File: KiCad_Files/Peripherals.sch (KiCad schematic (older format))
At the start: 20 parts, among them J3 MEM2075-00-140-01-A, U2 TCAN330G, U3 W25Q32JVSSIQ_TR

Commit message: Revert "Add shapes3D folder again"
This reverts commit 7987a310af828f940c17547aa6162ac2ebe2b018.
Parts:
- C11, C12, C13, C14, C15, C16, C17, C18, C19: symbol archive:Device_C_Small -> Device:C_Small
- D2: symbol archive:dk_TVS-Diodes_PESD2CAN_215 -> dk_TVS-Diodes:PESD2CAN_215
- J3: symbol archive:SamacSys_Parts_MEM2075-00-140-01-A -> SamacSys_Parts:MEM2075-00-140-01-A
- R5, R6, R7, R8, R9: symbol archive:Device_R_Small -> Device:R_Small
- RN1, RN2: symbol archive:Device_R_Pack04 -> Device:R_Pack04
- U2: symbol archive:Interface_CAN_LIN_TCAN330G -> Interface_CAN_LIN:TCAN330G
- U3: symbol archive:dk_Memory_W25Q32JVSSIQ_TR -> dk_Memory:W25Q32JVSSIQ_TR
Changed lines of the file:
@@
 $EndDescr
 $Comp
-L archive:power_+3.3V #PWR0115
+L power:+3.3V #PWR0115
 U 1 1 616DD3D7
 P 4400 5025
@@
 	4400 5025 4400 5100
 $Comp
-L archive:power_GND #PWR0119
+L power:GND #PWR0119
 U 1 1 616E5BF7
 P 4400 6750
@@
 	4400 6750 4400 6700
 $Comp
-L archive:Device_R_Pack04 RN2
+L Device:R_Pack04 RN2
 U 1 1 616ED35C
 P 3350 5425
@@
 	3550 5225 3550 5175
 $Comp
-L archive:power_+3.3V #PWR0120
+L power:+3.3V #PWR0120
 U 1 1 616ED34A
 P 3400 5100
@@
 $EndComp
 $Comp
-L archive:Device_R_Pack04 RN1
+L Device:R_Pack04 RN1
 U 1 1 616D8B8F
 P 2875 5425
@@
 	3075 5225 3075 5175
 $Comp
-L archive:power_+3.3V #PWR0121
+L power:+3.3V #PWR0121
 U 1 1 616DBD2E
 P 2925 5100
@@
 $EndComp
 $Comp
-L archive:Device_C_Small C17
+L Device:C_Small C17
 U 1 1 616FE025
 P 4600 5250
@@
 Connection ~ 4400 5100
 $Comp
-L archive:power_GND #PWR0122
+L power:GND #PWR0122
 U 1 1 616FF326
 P 4600 5450
@@
 SD_CARD_CD
 $Comp
-L archive:dk_Memory_W25Q32JVSSIQ_TR U3
+L dk_Memory:W25Q32JVSSIQ_TR U3
 U 1 1 614419FF
 P 9375 3825
@@
 $EndComp
 $Comp
-L archive:power_+3.3V #PWR0123
+L power:+3.3V #PWR0123
 U 1 1 6144F897
 P 9325 2925
@@
 $EndComp
 $Comp
-L archive:Device_C_Small C19
+L Device:C_Small C19
 U 1 1 6144FF8B
 P 9475 3125
@@
 $EndComp
 $Comp
-L archive:power_GND #PWR0124
+L power:GND #PWR0124
 U 1 1 61450343
 P 9475 3275
@@
 Connection ~ 9325 2975
 $Comp
-L archive:power_GND #PWR0125
+L power:GND #PWR0125
 U 1 1 6145B8A8
 P 9325 4325
@@
 	9325 4325 9325 4225
 $Comp
-L archive:Device_R_Small R9
+L Device:R_Small R9
 U 1 1 6145D636
 P 8825 3300
@@
 	9675 3875 9750 3875
 $Comp
-L archive:Device_C_Small C18
+L Device:C_Small C18
 U 1 1 61EAA5F8
 P 4975 5250
@@
 	4400 5100 4400 5500
 $Comp
-L archive:SamacSys_Parts_MEM2075-00-140-01-A J3
+L SamacSys_Parts:MEM2075-00-140-01-A J3
 U 1 1 616CDB72
 P 3750 5800
@@
 	3350 5175 3250 5175
 $Comp
-L archive:power_+3.3V #PWR0126
+L power:+3.3V #PWR0126
 U 1 1 61595989
 P 9750 3650
@@
 	9750 3650 9750 3775
 $Comp
-L archive:Interface_CAN_LIN_TCAN330G U2
+L Interface_CAN_LIN:TCAN330G U2
 U 1 1 61FFDC40
 P 3075 2425
@@
 $EndComp
 $Comp
-L archive:power_+3.3V #PWR0127
+L power:+3.3V #PWR0127
 U 1 1 620360A4
 P 3075 1425
@@
 $EndComp
 $Comp
-L archive:Device_C_Small C12
+L Device:C_Small C12
 U 1 1 620360AA
 P 3275 1625
@@
 	3275 1475 3275 1525
 $Comp
-L archive:power_GND #PWR0128
+L power:GND #PWR0128
 U 1 1 620360B2
 P 3275 1825
@@
 $EndComp
 $Comp
-L archive:Device_C_Small C13
+L Device:C_Small C13
 U 1 1 620360B8
 P 3650 1625
@@
 	3075 2900 3075 2825
 $Comp
-L archive:power_GND #PWR0129
+L power:GND #PWR0129
 U 1 1 6203C3B0
 P 3075 2900
@@
 $EndComp
 $Comp
-L archive:Device_R_Small R5
+L Device:R_Small R5
 U 1 1 620499E0
 P 2275 1875
@@
 $EndComp
 $Comp
-L archive:Device_R_Small R6
+L Device:R_Small R6
 U 1 1 620499E6
 P 2275 1975
@@
 CAN_RXD
 $Comp
-L archive:Device_C_Small C11
+L Device:C_Small C11
 U 1 1 620499EE
 P 2050 2150
@@
 $EndComp
 $Comp
-L archive:power_GND #PWR0130
+L power:GND #PWR0130
 U 1 1 620499F4
 P 2050 2275
@@
 CAN_H
 $Comp
-L archive:Device_R_Small R7
+L Device:R_Small R7
 U 1 1 62072AC4
 P 3800 2250
@@
 $EndComp
 $Comp
-L archive:Device_R_Small R8
+L Device:R_Small R8
 U 1 1 62072ACA
 P 3800 2650
@@
 	3800 2450 3800 2550
 $Comp
-L archive:Device_C_Small C16
+L Device:C_Small C16
 U 1 1 62072AD8
 P 4425 3000
@@
 $EndComp
 $Comp
-L archive:power_GND #PWR0131
+L power:GND #PWR0131
 U 1 1 62072ADE
 P 4425 3125
@@
 	4075 2450 3800 2450
 $Comp
-L archive:power_GND #PWR0132
+L power:GND #PWR0132
 U 1 1 62072AE8
 P 4075 2675
@@
 $EndComp
 $Comp
-L archive:Device_C_Small C14
+L Device:C_Small C14
 U 1 1 62072AEE
 P 4075 2575
@@
 CAN_L
 $Comp
-L archive:power_GND #PWR0133
+L power:GND #PWR0133
 U 1 1 62072B00
 P 4425 2325
@@
 	4425 2325 4425 2300
 $Comp
-L archive:Device_C_Small C15
+L Device:C_Small C15
 U 1 1 62072B07
 P 4425 2200
@@
 	3800 2050 4425 2050
 $Comp
-L archive:dk_TVS-Diodes_PESD2CAN_215 D2
+L dk_TVS-Diodes:PESD2CAN_215 D2
 U 1 1 62072B1A
 P 5075 2450
@@
 	4725 2850 5350 2850
 $Comp
-L archive:power_GND #PWR0134
+L power:GND #PWR0134
 U 1 1 62072B28
 P 5450 2500

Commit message: Archive Schematic
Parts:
- C11, C12, C13, C14, C15, C16, C17, C18, C19: symbol Device:C_Small -> archive:Device_C_Small
- D2: symbol dk_TVS-Diodes:PESD2CAN_215 -> archive:dk_TVS-Diodes_PESD2CAN_215
- J3: symbol SamacSys_Parts:MEM2075-00-140-01-A -> archive:SamacSys_Parts_MEM2075-00-140-01-A
- R5, R6, R7, R8, R9: symbol Device:R_Small -> archive:Device_R_Small
- RN1, RN2: symbol Device:R_Pack04 -> archive:Device_R_Pack04
- U2: symbol Interface_CAN_LIN:TCAN330G -> archive:Interface_CAN_LIN_TCAN330G
- U3: symbol dk_Memory:W25Q32JVSSIQ_TR -> archive:dk_Memory_W25Q32JVSSIQ_TR
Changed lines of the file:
@@
 $EndDescr
 $Comp
-L power:+3.3V #PWR0115
+L archive:power_+3.3V #PWR0115
 U 1 1 616DD3D7
 P 4400 5025
@@
 	4400 5025 4400 5100
 $Comp
-L power:GND #PWR0119
+L archive:power_GND #PWR0119
 U 1 1 616E5BF7
 P 4400 6750
@@
 	4400 6750 4400 6700
 $Comp
-L Device:R_Pack04 RN2
+L archive:Device_R_Pack04 RN2
 U 1 1 616ED35C
 P 3350 5425
@@
 	3550 5225 3550 5175
 $Comp
-L power:+3.3V #PWR0120
+L archive:power_+3.3V #PWR0120
 U 1 1 616ED34A
 P 3400 5100
@@
 $EndComp
 $Comp
-L Device:R_Pack04 RN1
+L archive:Device_R_Pack04 RN1
 U 1 1 616D8B8F
 P 2875 5425
@@
 	3075 5225 3075 5175
 $Comp
-L power:+3.3V #PWR0121
+L archive:power_+3.3V #PWR0121
 U 1 1 616DBD2E
 P 2925 5100
@@
 $EndComp
 $Comp
-L Device:C_Small C17
+L archive:Device_C_Small C17
 U 1 1 616FE025
 P 4600 5250
@@
 Connection ~ 4400 5100
 $Comp
-L power:GND #PWR0122
+L archive:power_GND #PWR0122
 U 1 1 616FF326
 P 4600 5450
@@
 SD_CARD_CD
 $Comp
-L dk_Memory:W25Q32JVSSIQ_TR U3
+L archive:dk_Memory_W25Q32JVSSIQ_TR U3
 U 1 1 614419FF
 P 9375 3825
@@
 $EndComp
 $Comp
-L power:+3.3V #PWR0123
+L archive:power_+3.3V #PWR0123
 U 1 1 6144F897
 P 9325 2925
@@
 $EndComp
 $Comp
-L Device:C_Small C19
+L archive:Device_C_Small C19
 U 1 1 6144FF8B
 P 9475 3125
@@
 $EndComp
 $Comp
-L power:GND #PWR0124
+L archive:power_GND #PWR0124
 U 1 1 61450343
 P 9475 3275
@@
 Connection ~ 9325 2975
 $Comp
-L power:GND #PWR0125
+L archive:power_GND #PWR0125
 U 1 1 6145B8A8
 P 9325 4325
@@
 	9325 4325 9325 4225
 $Comp
-L Device:R_Small R9
+L archive:Device_R_Small R9
 U 1 1 6145D636
 P 8825 3300
@@
 	9675 3875 9750 3875
 $Comp
-L Device:C_Small C18
+L archive:Device_C_Small C18
 U 1 1 61EAA5F8
 P 4975 5250
@@
 	4400 5100 4400 5500
 $Comp
-L SamacSys_Parts:MEM2075-00-140-01-A J3
+L archive:SamacSys_Parts_MEM2075-00-140-01-A J3
 U 1 1 616CDB72
 P 3750 5800
@@
 	3350 5175 3250 5175
 $Comp
-L power:+3.3V #PWR0126
+L archive:power_+3.3V #PWR0126
 U 1 1 61595989
 P 9750 3650
@@
 	9750 3650 9750 3775
 $Comp
-L Interface_CAN_LIN:TCAN330G U2
+L archive:Interface_CAN_LIN_TCAN330G U2
 U 1 1 61FFDC40
 P 3075 2425
@@
 $EndComp
 $Comp
-L power:+3.3V #PWR0127
+L archive:power_+3.3V #PWR0127
 U 1 1 620360A4
 P 3075 1425
@@
 $EndComp
 $Comp
-L Device:C_Small C12
+L archive:Device_C_Small C12
 U 1 1 620360AA
 P 3275 1625
@@
 	3275 1475 3275 1525
 $Comp
-L power:GND #PWR0128
+L archive:power_GND #PWR0128
 U 1 1 620360B2
 P 3275 1825
@@
 $EndComp
 $Comp
-L Device:C_Small C13
+L archive:Device_C_Small C13
 U 1 1 620360B8
 P 3650 1625
@@
 	3075 2900 3075 2825
 $Comp
-L power:GND #PWR0129
+L archive:power_GND #PWR0129
 U 1 1 6203C3B0
 P 3075 2900
@@
 $EndComp
 $Comp
-L Device:R_Small R5
+L archive:Device_R_Small R5
 U 1 1 620499E0
 P 2275 1875
@@
 $EndComp
 $Comp
-L Device:R_Small R6
+L archive:Device_R_Small R6
 U 1 1 620499E6
 P 2275 1975
@@
 CAN_RXD
 $Comp
-L Device:C_Small C11
+L archive:Device_C_Small C11
 U 1 1 620499EE
 P 2050 2150
@@
 $EndComp
 $Comp
-L power:GND #PWR0130
+L archive:power_GND #PWR0130
 U 1 1 620499F4
 P 2050 2275
@@
 CAN_H
 $Comp
-L Device:R_Small R7
+L archive:Device_R_Small R7
 U 1 1 62072AC4
 P 3800 2250
@@
 $EndComp
 $Comp
-L Device:R_Small R8
+L archive:Device_R_Small R8
 U 1 1 62072ACA
 P 3800 2650
@@
 	3800 2450 3800 2550
 $Comp
-L Device:C_Small C16
+L archive:Device_C_Small C16
 U 1 1 62072AD8
 P 4425 3000
@@
 $EndComp
 $Comp
-L power:GND #PWR0131
+L archive:power_GND #PWR0131
 U 1 1 62072ADE
 P 4425 3125
@@
 	4075 2450 3800 2450
 $Comp
-L power:GND #PWR0132
+L archive:power_GND #PWR0132
 U 1 1 62072AE8
 P 4075 2675
@@
 $EndComp
 $Comp
-L Device:C_Small C14
+L archive:Device_C_Small C14
 U 1 1 62072AEE
 P 4075 2575
@@
 CAN_L
 $Comp
-L power:GND #PWR0133
+L archive:power_GND #PWR0133
 U 1 1 62072B00
 P 4425 2325
@@
 	4425 2325 4425 2300
 $Comp
-L Device:C_Small C15
+L archive:Device_C_Small C15
 U 1 1 62072B07
 P 4425 2200
@@
 	3800 2050 4425 2050
 $Comp
-L dk_TVS-Diodes:PESD2CAN_215 D2
+L archive:dk_TVS-Diodes_PESD2CAN_215 D2
 U 1 1 62072B1A
 P 5075 2450
@@
 	4725 2850 5350 2850
 $Comp
-L power:GND #PWR0134
+L archive:power_GND #PWR0134
 U 1 1 62072B28
 P 5450 2500

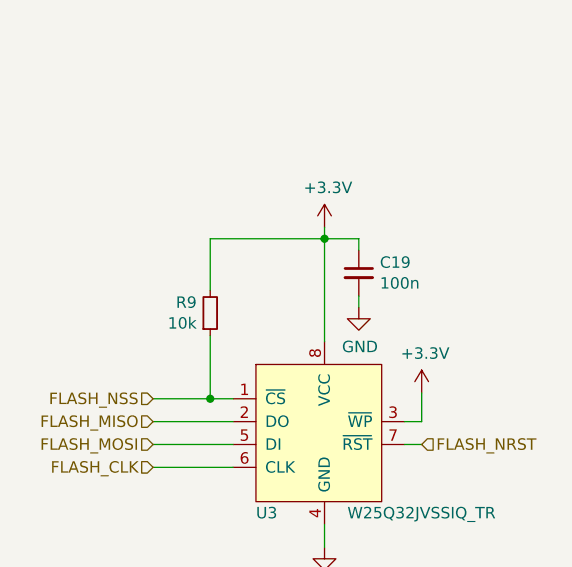
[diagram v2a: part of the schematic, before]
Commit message: Reroutes voltage reference selector trace for better aesthetics.
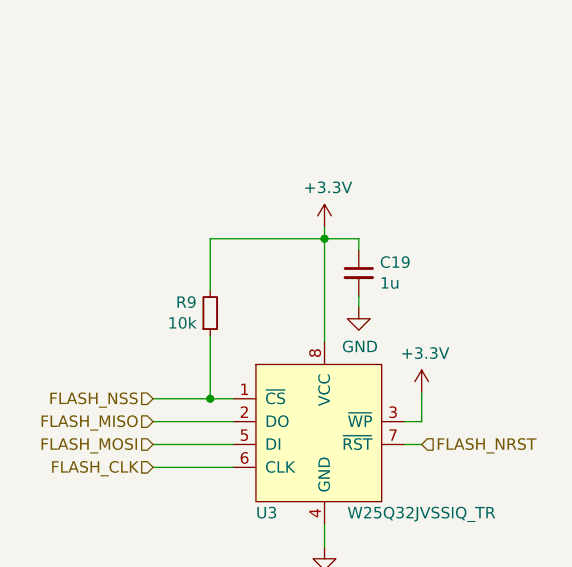
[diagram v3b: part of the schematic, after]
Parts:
- C19: value 100n -> 1u
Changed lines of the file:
@@
 P 9475 3125
 F 0 "C19" H 9567 3171 50  0000 L CNN
-F 1 "100n" H 9567 3080 50  0000 L CNN
+F 1 "1u" H 9567 3080 50  0000 L CNN
 F 2 "Capacitor_SMD:C_0805_2012Metric" H 9475 3125 50  0001 C CNN
 F 3 "~" H 9475 3125 50  0001 C CNN
